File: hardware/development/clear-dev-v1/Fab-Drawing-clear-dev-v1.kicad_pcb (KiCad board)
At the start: 2 copper layers, 76.2 x 73.8 mm, 80 parts, among them J1 USB_B_Micro, J10 Conn_01x28_Pin, J11 Conn_01x28_Pin, J12 Conn_01x02_Pin, J2 Conn_01x02_Pin, J3 Conn_01x02_Pin, J4 Conn_01x03_Pin, J5 Conn_01x02_Pin, J6 Conn_01x02_Pin, J7 Conn_01x06_Pin, J8 Conn_01x02_Pin, J9 Conn_01x02_Pin, SW1 SW_Push - SKQGADE010, T1 Logo, T2 Logo, U1 FT232H, U10 DS1086LU, U2 SN74LVC1G125DCKR, U3 SN74LVC1G125DCKR, U4 SN74LVC1G125DCKR, U5 TAR5SxxU, U6 TAR5SxxU, U7 W25Q32FVSS, U8 M.2-CONNECTOR-E, U9 TMUX4053-BQB, X1 DSC6001_10MHZ, Y1 12MHz

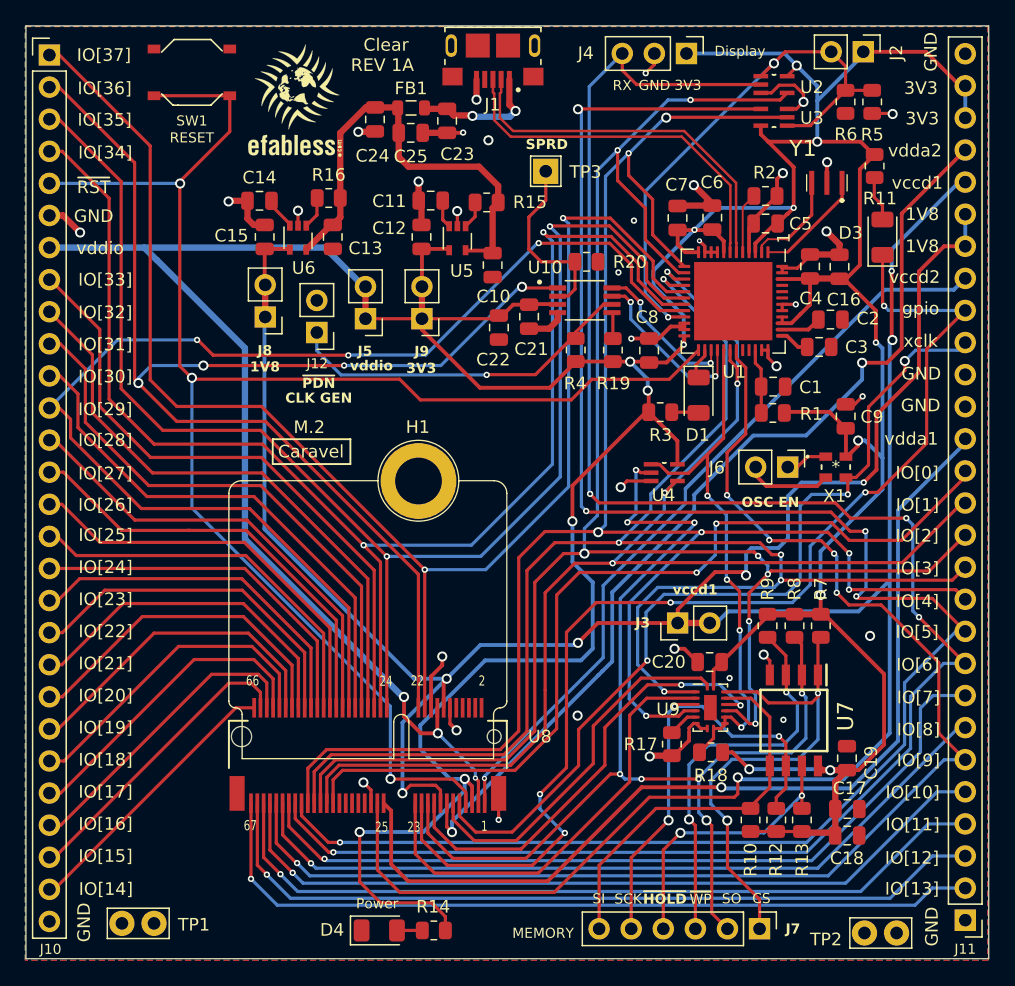
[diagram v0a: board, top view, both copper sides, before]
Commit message: update clear dev board to REV 1B after layout review
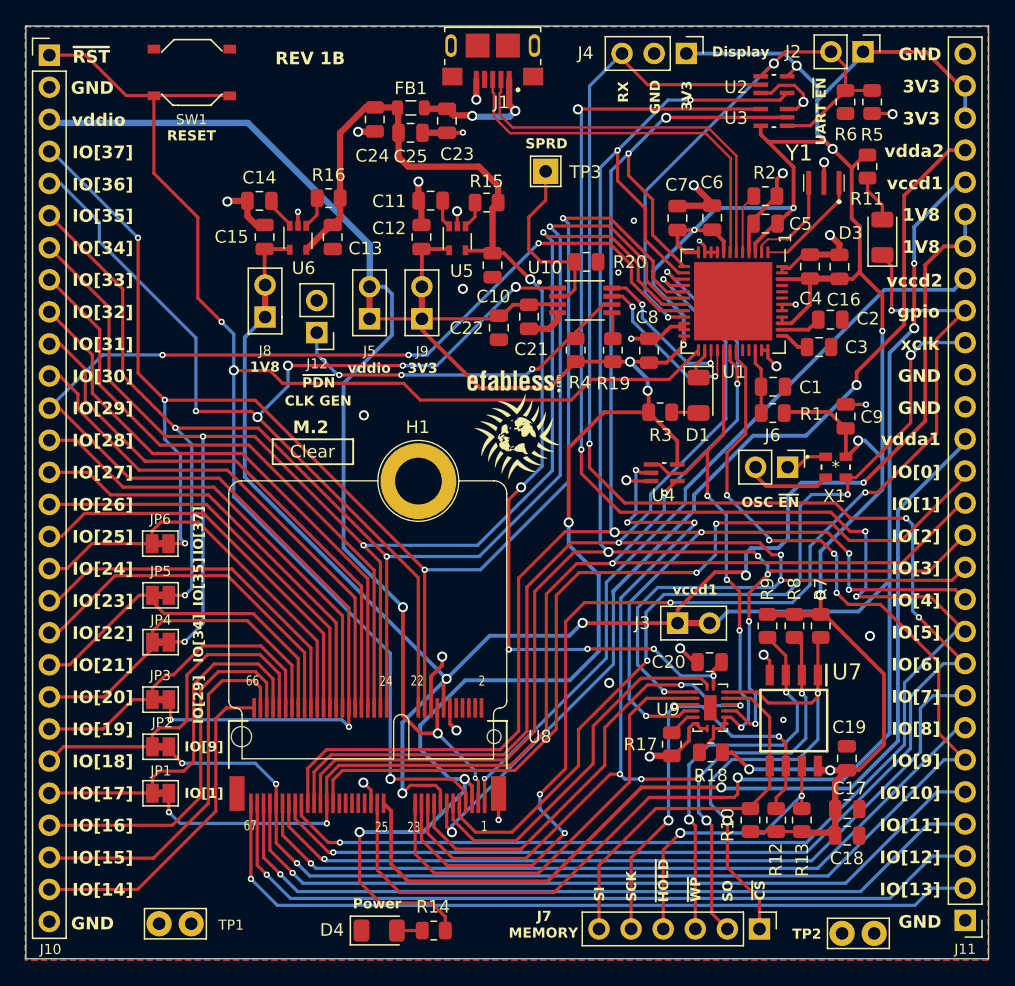
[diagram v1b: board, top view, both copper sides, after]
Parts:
- added JP1: SolderJumper_2_Bridged, Jumper:SolderJumper-2_P1.3mm_Bridged_Pad1.0x1.5mm, F.Cu at (105.7, 178.4)
- added JP2: SolderJumper_2_Bridged, Jumper:SolderJumper-2_P1.3mm_Bridged_Pad1.0x1.5mm, F.Cu at (105.7, 174.7)
- added JP3: SolderJumper_2_Bridged, Jumper:SolderJumper-2_P1.3mm_Bridged_Pad1.0x1.5mm, F.Cu at (105.7, 171.0)
- added JP4: SolderJumper_2_Bridged, Jumper:SolderJumper-2_P1.3mm_Bridged_Pad1.0x1.5mm, F.Cu at (105.7, 166.5)
- added JP5: SolderJumper_2_Bridged, Jumper:SolderJumper-2_P1.3mm_Bridged_Pad1.0x1.5mm, F.Cu at (105.7, 162.7)
- added JP6: SolderJumper_2_Bridged, Jumper:SolderJumper-2_P1.3mm_Bridged_Pad1.0x1.5mm, F.Cu at (105.7, 158.7)
- J3, J5, J8, J9: footprint Connector_PinHeader_2.54mm:PinHeader_1x02_P2.54mm_Vertical -> Caravel_Board:Shorted_PinHeader_1x02_P2.54mm_Vertical
- moved T1 32.7 mm to (133.9, 150.2)
- moved T2 25.5 mm to (133.6, 145.8)
- moved TP1 2.94 mm to (108.1, 188.7)
- moved TP2 1.77 mm to (162.2, 189.5)
- moved R11 0.57 mm to (161.6, 128.8)
- moved J5 0.32 mm to (122.2, 140.9)
- moved Y1 0.24 mm to (158.2, 130.1)
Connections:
- C1 pad 1: GND -> (no net)
- C1 pad 2: /~{FTDI_RST} -> (no net)
- C10 pad 1: GND -> (no net)
- C10 pad 2: +5V -> (no net)
- C11 pad 1: /Noise_3V3 -> (no net)
- C11 pad 2: GND -> (no net)
- C12 pad 1: GND -> (no net)
- C12 pad 2: +3V3 -> (no net)
- C13 pad 1: GND -> (no net)
- C13 pad 2: +5V -> (no net)
- C14 pad 1: /Noise_1V8 -> (no net)
- C14 pad 2: GND -> (no net)
- C15 pad 1: GND -> (no net)
- C15 pad 2: +1V8 -> (no net)
- C16 pad 1: +3V3 -> (no net)
- C16 pad 2: GND -> (no net)
- C17 pad 1: GND -> (no net)
- C17 pad 2: +3V3 -> (no net)
- C18 pad 1: +3V3 -> (no net)
- C18 pad 2: GND -> (no net)
- C19 pad 1: +3V3 -> (no net)
- C19 pad 2: GND -> (no net)
- C2 pad 1: GND -> (no net)
- C2 pad 2: /VCCCORE -> (no net)
- C20 pad 1: GND -> (no net)
- C20 pad 2: +3V3 -> (no net)
- C21 pad 1: GND -> (no net)
- C21 pad 2: +3V3 -> (no net)
- C22 pad 1: GND -> (no net)
- C22 pad 2: +3V3 -> (no net)
- C23 pad 1: VBUS -> (no net)
- C23 pad 2: GND -> (no net)
- C24 pad 1: GND -> (no net)
- C24 pad 2: +5V -> (no net)
- C25 pad 1: GND -> (no net)
- C25 pad 2: +5V -> (no net)
- C3 pad 1: GND -> (no net)
- C3 pad 2: /VCCA -> (no net)
- C4 pad 1: GND -> (no net)
- C4 pad 2: +3V3 -> (no net)
- C5 pad 1: GND -> (no net)
- C5 pad 2: +3V3 -> (no net)
- C6 pad 1: GND -> (no net)
- C6 pad 2: +3V3 -> (no net)
- C7 pad 1: GND -> (no net)
- C7 pad 2: +3V3 -> (no net)
- C8 pad 1: GND -> (no net)
- C8 pad 2: +3V3 -> (no net)
- C9 pad 1: GND -> (no net)
- C9 pad 2: +3V3 -> (no net)
- D1 pad 1: /ACBUS2 -> (no net)
- D1 pad 2: Net-(D1-A) -> (no net)
- D3 pad 1: /gpio -> (no net)
- D3 pad 2: Net-(D3-A) -> (no net)
- D4 pad 1: GND -> (no net)
- D4 pad 2: Net-(D4-A) -> (no net)
- FB1 pad 1: VBUS -> (no net)
- FB1 pad 2: +5V -> (no net)
- J1 pad 1: VBUS -> (no net)
- J1 pad 2: /FTDI_D- -> (no net)
- J1 pad 3: /FTDI_D+ -> (no net)
- J1 pad 4: unconnected-(J1-ID-Pad4) -> (no net)
- J1 pad 5: GND -> (no net)
- J1 pad 6: unconnected-(J1-Shield-Pad6) -> (no net)
- J10 pad 1: /ADBUS4 -> (no net)
- J10 pad 10: /mprj_io[31] -> (no net)
- J10 pad 11: /mprj_io[30] -> (no net)
- J10 pad 12: /ADBUS7 -> (no net)
- J10 pad 13: /mprj_io[28] -> (no net)
- J10 pad 14: /mprj_io[27] -> (no net)
- J10 pad 15: /mprj_io[26] -> (no net)
- J10 pad 16: /mprj_io[25] -> (no net)
- J10 pad 17: /mprj_io[24] -> (no net)
- J10 pad 18: /mprj_io[23] -> (no net)
- J10 pad 19: /mprj_io[22] -> (no net)
- J10 pad 2: /CLK_GEN -> (no net)
- J10 pad 20: /mprj_io[21] -> (no net)
- J10 pad 21: /mprj_io[20] -> (no net)
- J10 pad 22: /mprj_io[19] -> (no net)
- J10 pad 23: /mprj_io[18] -> (no net)
- J10 pad 24: /mprj_io[17] -> (no net)
- J10 pad 25: /mprj_io[16] -> (no net)
- J10 pad 26: /mprj_io[15] -> (no net)
- J10 pad 27: /mprj_io[14] -> (no net)
- J10 pad 28: GND -> (no net)
- J10 pad 3: /ADBUS5 -> (no net)
- J10 pad 4: /ADBUS6 -> (no net)
- J10 pad 5: /ACBUS1 -> (no net)
- J10 pad 6: GND -> (no net)
- J10 pad 7: +3V3 -> (no net)
- J10 pad 8: /mprj_io[33] -> (no net)
- J10 pad 9: /mprj_io[32] -> (no net)
- J11 pad 1: GND -> (no net)
- J11 pad 10: /mprj_io[5]_ser_rx -> (no net)
- J11 pad 11: /USB_SCK_TXD -> (no net)
- J11 pad 12: /USB_CS1 -> (no net)
- J11 pad 13: /USB_SO_RXD -> (no net)
- J11 pad 14: /ACBUS6 -> (no net)
- J11 pad 15: /mprj_io[0] -> (no net)
- J11 pad 16: /vdda1 -> (no net)
- J11 pad 17: GND -> (no net)
- J11 pad 18: GND -> (no net)
- J11 pad 19: /xclk -> (no net)
- J11 pad 2: /mprj_io[13] -> (no net)
- J11 pad 20: /gpio -> (no net)
- J11 pad 21: /vccd2 -> (no net)
- J11 pad 22: +1V8 -> (no net)
- J11 pad 23: +1V8 -> (no net)
- J11 pad 24: +1V8 -> (no net)
- J11 pad 25: /vdda2 -> (no net)
- J11 pad 26: +3V3 -> (no net)
- J11 pad 27: +3V3 -> (no net)
- J11 pad 28: GND -> (no net)
- J11 pad 3: /mprj_io[12] -> (no net)
- J11 pad 4: /mprj_io[11] -> (no net)
- J11 pad 5: /mprj_io[10] -> (no net)
- J11 pad 6: /ACBUS7 -> (no net)
- J11 pad 7: /mprj_io[8] -> (no net)
- J11 pad 8: /mprj_io[7] -> (no net)
- J11 pad 9: /mprj_io[6]_ser_tx -> (no net)
- J12 pad 1: /~{PDN} -> (no net)
- J12 pad 2: GND -> (no net)
- J2 pad 1: +3V3 -> (no net)
- J2 pad 2: /ACBUS0 -> (no net)
- J3 pad 1: +1V8 -> (no net)
- J3 pad 2: +1V8 -> (no net)
- J4 pad 1: +3V3 -> (no net)
- J4 pad 2: GND -> (no net)
- J4 pad 3: /mprj_io[6]_ser_tx -> (no net)
- J5 pad 1: +3V3 -> (no net)
- J5 pad 2: +3V3 -> (no net)
- J6 pad 1: /OSC_EN -> (no net)
- J6 pad 2: GND -> (no net)
- J7 pad 1: /~{MEM_CS} -> (no net)
- J7 pad 2: /Caravel_D1 -> (no net)
- J7 pad 3: /~{MEM_WP} -> (no net)
- J7 pad 4: /~{MEM_HOLD} -> (no net)
- J7 pad 5: /MEM_SCK -> (no net)
- J7 pad 6: /MEM_SI -> (no net)
- J8 pad 1: +1V8 -> (no net)
- J8 pad 2: +1V8 -> (no net)
- J9 pad 1: +3V3 -> (no net)
- J9 pad 2: +3V3 -> (no net)
- R1 pad 1: /~{FTDI_RST} -> (no net)
- R1 pad 2: +3V3 -> (no net)
- R10 pad 1: /MEM_SI -> (no net)
- R10 pad 2: +3V3 -> (no net)
- R11 pad 1: +3V3 -> (no net)
- R11 pad 2: Net-(D3-A) -> (no net)
- R12 pad 1: /MEM_SCK -> (no net)
- R12 pad 2: +3V3 -> (no net)
- R13 pad 1: /~{MEM_HOLD} -> (no net)
- R13 pad 2: +3V3 -> (no net)
- R14 pad 1: +3V3 -> (no net)
- R14 pad 2: Net-(D4-A) -> (no net)
- R15 pad 1: Net-(U5-Control) -> (no net)
- R15 pad 2: +5V -> (no net)
- R16 pad 1: Net-(U6-Control) -> (no net)
- R16 pad 2: +5V -> (no net)
- R17 pad 1: GND -> (no net)
- R17 pad 2: Net-(U9-~{EN}) -> (no net)
- R18 pad 1: +3V3 -> (no net)
- R18 pad 2: /ACBUS5 -> (no net)
- R19 pad 1: +3V3 -> (no net)
- R19 pad 2: Net-(U10-OE) -> (no net)
- R2 pad 1: GND -> (no net)
- R2 pad 2: Net-(U1-REF) -> (no net)
- R20 pad 1: GND -> (no net)
- R20 pad 2: /SPRD -> (no net)
- R3 pad 1: Net-(D1-A) -> (no net)
- R3 pad 2: +3V3 -> (no net)
- R4 pad 1: +3V3 -> (no net)
- R4 pad 2: /~{PDN} -> (no net)
- R5 pad 1: GND -> (no net)
- R5 pad 2: /ACBUS0 -> (no net)
- R6 pad 1: GND -> (no net)
- R6 pad 2: /ACBUS0 -> (no net)
- R7 pad 1: /~{MEM_CS} -> (no net)
- R7 pad 2: +3V3 -> (no net)
- R8 pad 1: /Caravel_D1 -> (no net)
- R8 pad 2: +3V3 -> (no net)
- R9 pad 1: /~{MEM_WP} -> (no net)
- R9 pad 2: +3V3 -> (no net)
- SW1 pad 1: /ACBUS1 -> (no net)
- SW1 pad 2: GND -> (no net)
- TP1 pad 1: GND -> (no net)
- TP2 pad 1: GND -> (no net)
- TP3 pad 1: /SPRD -> (no net)
- U1 pad 1: Net-(U1-XCSI) -> (no net)
- U1 pad 10: GND -> (no net)
- U1 pad 11: GND -> (no net)
- U1 pad 12: +3V3 -> (no net)
- U1 pad 13: /USB_SCK_TXD -> (no net)
- U1 pad 14: /USB_SO_RXD -> (no net)
- U1 pad 15: /ACBUS6 -> (no net)
- U1 pad 16: /USB_CS1 -> (no net)
- U1 pad 17: /ADBUS4 -> (no net)
- U1 pad 18: /ADBUS5 -> (no net)
- U1 pad 19: /ADBUS6 -> (no net)
- U1 pad 2: Net-(U1-XCSO) -> (no net)
- U1 pad 20: /ADBUS7 -> (no net)
- U1 pad 21: /ACBUS0 -> (no net)
- U1 pad 22: GND -> (no net)
- U1 pad 23: GND -> (no net)
- U1 pad 24: +3V3 -> (no net)
- U1 pad 25: /ACBUS1 -> (no net)
- U1 pad 26: /ACBUS2 -> (no net)
- U1 pad 27: /ACBUS3 -> (no net)
- U1 pad 28: /ACBUS4 -> (no net)
- U1 pad 29: /ACBUS5 -> (no net)
- U1 pad 3: +3V3 -> (no net)
- U1 pad 30: /ACBUS6 -> (no net)
- U1 pad 31: /ACBUS7 -> (no net)
- U1 pad 32: unconnected-(U1-ACBUS8-Pad32) -> (no net)
- U1 pad 33: unconnected-(U1-ACBUS9-Pad33) -> (no net)
- U1 pad 34: /~{FTDI_RST} -> (no net)
- U1 pad 35: GND -> (no net)
- U1 pad 36: GND -> (no net)
- U1 pad 37: /VCCA -> (no net)
- U1 pad 38: /VCCCORE -> (no net)
- U1 pad 39: +3V3 -> (no net)
- U1 pad 4: GND -> (no net)
- U1 pad 40: +3V3 -> (no net)
- U1 pad 41: GND -> (no net)
- U1 pad 42: GND -> (no net)
- U1 pad 43: unconnected-(U1-EEDATA-Pad43) -> (no net)
- U1 pad 44: unconnected-(U1-EECLK-Pad44) -> (no net)
- U1 pad 45: unconnected-(U1-EECS-Pad45) -> (no net)
- U1 pad 46: +3V3 -> (no net)
- U1 pad 47: GND -> (no net)
- U1 pad 48: GND -> (no net)
- U1 pad 5: Net-(U1-REF) -> (no net)
- U1 pad 6: /FTDI_D- -> (no net)
- U1 pad 7: /FTDI_D+ -> (no net)
- U1 pad 8: +3V3 -> (no net)
- U1 pad 9: GND -> (no net)
- U10 pad 1: /CLK_GEN -> (no net)
- U10 pad 2: /SPRD -> (no net)
- U10 pad 3: +3V3 -> (no net)
- U10 pad 4: GND -> (no net)
- U10 pad 5: Net-(U10-OE) -> (no net)
- U10 pad 6: /~{PDN} -> (no net)
- U10 pad 7: /ACBUS4 -> (no net)
- U10 pad 8: /ACBUS3 -> (no net)
- U2 pad 1: /ACBUS0 -> (no net)
- U2 pad 2: /mprj_io[6]_ser_tx -> (no net)
- U2 pad 3: GND -> (no net)
- U2 pad 4: /USB_SO_RXD -> (no net)
- U2 pad 5: +3V3 -> (no net)
- U3 pad 1: /ACBUS0 -> (no net)
- U3 pad 2: /USB_SCK_TXD -> (no net)
- U3 pad 3: GND -> (no net)
- U3 pad 4: /mprj_io[5]_ser_rx -> (no net)
- U3 pad 5: +3V3 -> (no net)
- U4 pad 1: /ACBUS5 -> (no net)
- U4 pad 2: /Caravel_D1 -> (no net)
- U4 pad 3: GND -> (no net)
- U4 pad 4: /ACBUS6 -> (no net)
- U4 pad 5: +3V3 -> (no net)
- U5 pad 1: Net-(U5-Control) -> (no net)
- U5 pad 2: GND -> (no net)
- U5 pad 3: /Noise_3V3 -> (no net)
- U5 pad 4: +3V3 -> (no net)
- U5 pad 5: +5V -> (no net)
- U6 pad 1: Net-(U6-Control) -> (no net)
- U6 pad 2: GND -> (no net)
- U6 pad 3: /Noise_1V8 -> (no net)
- U6 pad 4: +1V8 -> (no net)
- U6 pad 5: +5V -> (no net)
- U7 pad 1: /~{MEM_CS} -> (no net)
- U7 pad 2: /Caravel_D1 -> (no net)
- U7 pad 3: /~{MEM_WP} -> (no net)
- U7 pad 4: GND -> (no net)
- U7 pad 5: /MEM_SI -> (no net)
- U7 pad 6: /MEM_SCK -> (no net)
- U7 pad 7: /~{MEM_HOLD} -> (no net)
- U7 pad 8: +3V3 -> (no net)
- U8 pad 1: /vccd2 -> (no net)
- U8 pad 10: unconnected-(U8-P10-Pad10) -> (no net)
- U8 pad 11: /Caravel_CSB -> (no net)
- U8 pad 12: GND -> (no net)
- U8 pad 13: /vdda2 -> (no net)
- U8 pad 14: +1V8 -> (no net)
- U8 pad 15: +1V8 -> (no net)
- U8 pad 16: +3V3 -> (no net)
- U8 pad 17: /Caravel_D0 -> (no net)
- U8 pad 18: GND -> (no net)
- U8 pad 19: /Caravel_D1 -> (no net)
- U8 pad 2: unconnected-(U8-P2-Pad2) -> (no net)
- U8 pad 20: /ADBUS4 -> (no net)
- U8 pad 21: /gpio -> (no net)
- U8 pad 22: /CLK_GEN -> (no net)
- U8 pad 23: /Caravel_SCK -> (no net)
- U8 pad 3: +3V3 -> (no net)
- U8 pad 32: /ADBUS5 -> (no net)
- U8 pad 33: /vdda1 -> (no net)
- U8 pad 34: /ADBUS6 -> (no net)
- U8 pad 35: +1V8 -> (no net)
- U8 pad 36: /mprj_io[33] -> (no net)
- U8 pad 37: GND -> (no net)
- U8 pad 38: /mprj_io[32] -> (no net)
- U8 pad 39: unconnected-(U8-P31-Pad39) -> (no net)
- U8 pad 4: unconnected-(U8-P4-Pad4) -> (no net)
- U8 pad 40: /mprj_io[31] -> (no net)
- U8 pad 41: unconnected-(U8-P33-Pad41) -> (no net)
- U8 pad 42: /mprj_io[30] -> (no net)
- U8 pad 43: unconnected-(U8-P35-Pad43) -> (no net)
- U8 pad 44: /ADBUS7 -> (no net)
- U8 pad 45: unconnected-(U8-P37-Pad45) -> (no net)
- U8 pad 46: /mprj_io[28] -> (no net)
- U8 pad 47: unconnected-(U8-P39-Pad47) -> (no net)
- U8 pad 48: /mprj_io[27] -> (no net)
- U8 pad 49: /mprj_io[0] -> (no net)
- U8 pad 5: +3V3 -> (no net)
- U8 pad 50: /mprj_io[26] -> (no net)
- U8 pad 51: /ACBUS6 -> (no net)
- U8 pad 52: /mprj_io[25] -> (no net)
- U8 pad 53: /USB_SO_RXD -> (no net)
- U8 pad 54: /mprj_io[24] -> (no net)
- U8 pad 55: /USB_CS1 -> (no net)
- U8 pad 56: /mprj_io[23] -> (no net)
- U8 pad 57: /USB_SCK_TXD -> (no net)
- U8 pad 58: /mprj_io[22] -> (no net)
- U8 pad 59: /mprj_io[5]_ser_rx -> (no net)
- U8 pad 6: unconnected-(U8-P6-Pad6) -> (no net)
- U8 pad 60: /mprj_io[21] -> (no net)
- U8 pad 61: /mprj_io[6]_ser_tx -> (no net)
- U8 pad 62: /mprj_io[20] -> (no net)
- U8 pad 63: /mprj_io[7] -> (no net)
- U8 pad 64: /mprj_io[19] -> (no net)
- U8 pad 65: /mprj_io[8] -> (no net)
- U8 pad 66: /mprj_io[18] -> (no net)
- U8 pad 67: /ACBUS7 -> (no net)
- U8 pad 68: /mprj_io[17] -> (no net)
- U8 pad 69: /mprj_io[10] -> (no net)
- U8 pad 7: /ACBUS1 -> (no net)
- U8 pad 70: /mprj_io[16] -> (no net)
- U8 pad 71: /mprj_io[11] -> (no net)
- U8 pad 72: /mprj_io[15] -> (no net)
- U8 pad 73: /mprj_io[12] -> (no net)
- U8 pad 74: /mprj_io[14] -> (no net)
- U8 pad 75: /mprj_io[13] -> (no net)
- U8 pad 8: unconnected-(U8-P8-Pad8) -> (no net)
- U8 pad 9: /xclk -> (no net)
- U8 pad A1: GND -> (no net)
- U8 pad A2: GND -> (no net)
- U9 pad 1: /Caravel_CSB -> (no net)
- U9 pad 10: /ACBUS5 -> (no net)
- U9 pad 11: /ACBUS5 -> (no net)
- U9 pad 12: /USB_SO_RXD -> (no net)
- U9 pad 13: /Caravel_D0 -> (no net)
- U9 pad 14: /MEM_SI -> (no net)
- U9 pad 15: /~{MEM_CS} -> (no net)
- U9 pad 16: +3V3 -> (no net)
- U9 pad 2: /USB_CS1 -> (no net)
- U9 pad 3: /Caravel_SCK -> (no net)
- U9 pad 4: /MEM_SCK -> (no net)
- U9 pad 5: /USB_SCK_TXD -> (no net)
- U9 pad 6: Net-(U9-~{EN}) -> (no net)
- U9 pad 7: GND -> (no net)
- U9 pad 8: GND -> (no net)
- U9 pad 9: /ACBUS5 -> (no net)
- X1 pad 1: /OSC_EN -> (no net)
- X1 pad 2: GND -> (no net)
- X1 pad 3: /xclk -> (no net)
- X1 pad 4: +3V3 -> (no net)
- Y1 pad 1: Net-(U1-XCSI) -> (no net)
- Y1 pad 2: GND -> (no net)
- Y1 pad 3: Net-(U1-XCSO) -> (no net)
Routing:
- net (no net): track 0.00 -> 4576.3 mm, vias 0 -> 186
- net +3V3: track 416.7 -> 0.00 mm, vias 18 -> 0
- net +1V8: track 246.8 -> 0.00 mm, vias 8 -> 0
- net /mprj_io[6]_ser_tx: track 151.9 -> 0.00 mm, vias 4 -> 0
- net /USB_SCK_TXD: track 151.7 -> 0.00 mm, vias 7 -> 0
- net /mprj_io[5]_ser_rx: track 148.9 -> 0.00 mm, vias 5 -> 0
- net /USB_SO_RXD: track 145.7 -> 0.00 mm, vias 7 -> 0
- net /ACBUS1: track 128.6 -> 0.00 mm, vias 3 -> 0
- net /USB_CS1: track 122.0 -> 0.00 mm, vias 5 -> 0
- net /ADBUS4: track 116.7 -> 0.00 mm, vias 2 -> 0
- net /ADBUS5: track 113.0 -> 0.00 mm, vias 2 -> 0
- net /ADBUS6: track 111.1 -> 0.00 mm, vias 2 -> 0
- net /ACBUS7: track 107.5 -> 0.00 mm, vias 5 -> 0
- net /ACBUS6: track 102.5 -> 0.00 mm, vias 4 -> 0
- net /CLK_GEN: track 102.4 -> 0.00 mm, vias 4 -> 0
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- added copper zone on B.Cu, net (none)
- added copper zone on F.Cu, net (none)
- removed copper zone on B.Cu, net GND
- removed copper zone on F.Cu, net GND
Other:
- board text added: "H1"
- board text added: "J1"
- board text added: "OSC ~{EN}"
- board text added: "REV 1B"
- board text added: "SW1"
- board text added: "U10"
- board text added: "U2"
- board text added: "U3"
- board text added: "U4"
- board text added: "UART ~{EN}"
- board text added: "X1"
- board text added: "~{CS}"
- board text removed: "CS"
- board text removed: "Caravel"
- board text removed: "OSC EN"
- board text removed: "REV 1A"
